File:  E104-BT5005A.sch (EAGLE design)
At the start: 5 parts

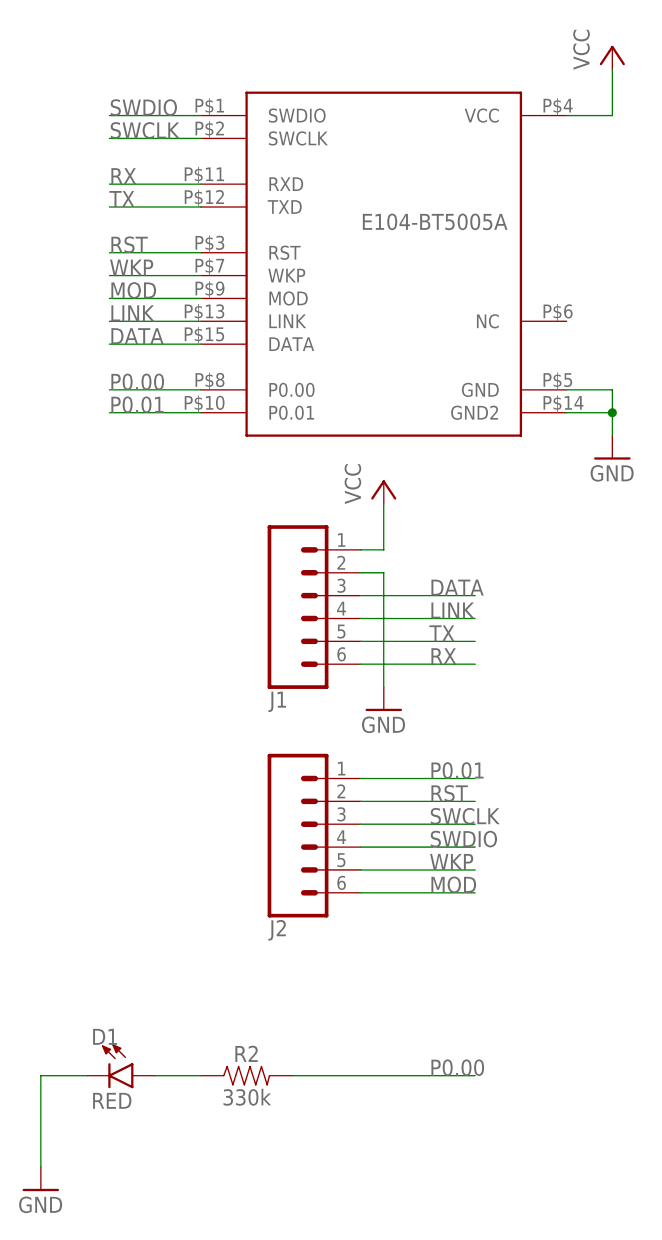
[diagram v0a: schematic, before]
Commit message: v2 fixes, errors with part library
the original module library had errors. fixed module and silkscreen, added eagle library for ble module
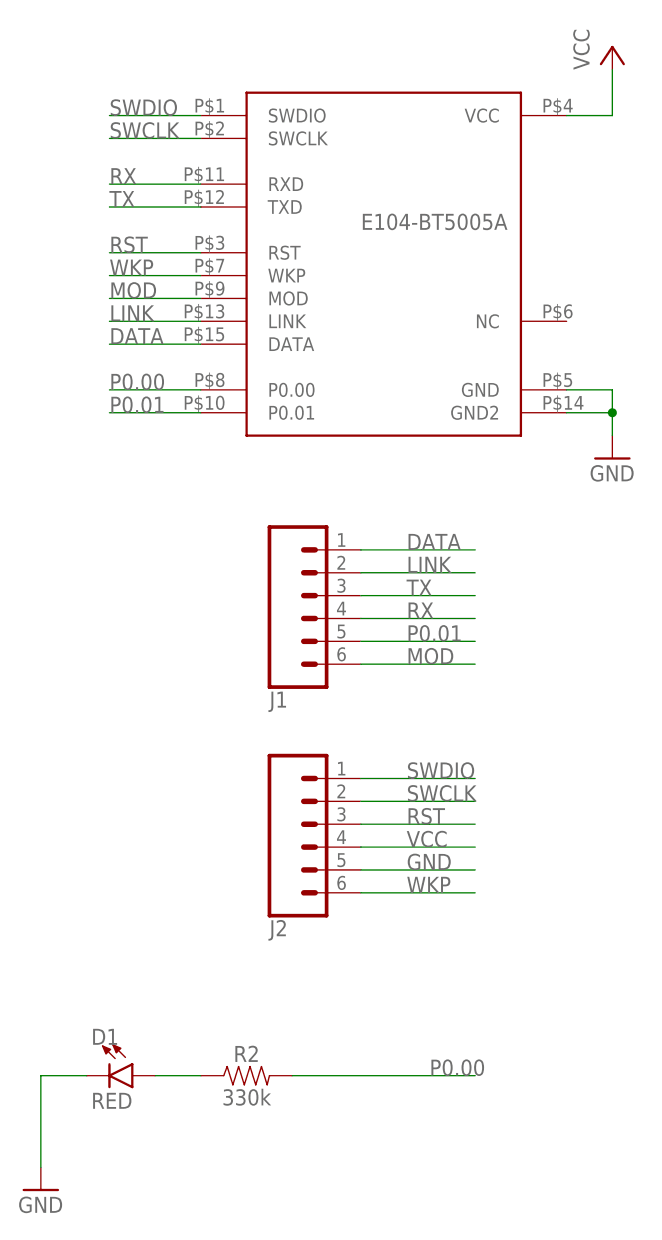
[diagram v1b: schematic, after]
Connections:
- net DATA: now also J1.1; no longer J1.3
- net GND: now also J2.5; no longer J1.2
- net LINK: now also J1.2; no longer J1.4
- net MOD: now also J1.6; no longer J2.6
- net P0.01: now also J1.5; no longer J2.1
- net RST: now also J2.3; no longer J2.2
- net RX: now also J1.4; no longer J1.6
- net SWCLK: now also J2.2; no longer J2.3
- net SWDIO: now also J2.1; no longer J2.4
- net TX: now also J1.3; no longer J1.5
- net VCC: now also J2.4; no longer J1.1
- net WKP: now also J2.6; no longer J2.5
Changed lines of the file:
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@@
 <part name="GND1" library="supply1" library_urn="urn:adsk.eagle:library:371" deviceset="GND" device=""/>
 <part name="J1" library="SparkFun-Connectors" library_urn="urn:adsk.eagle:library:513" deviceset="CONN_06" device="SILK_FEMALE_PTH" package3d_urn="urn:adsk.eagle:package:38009/1"/>
-<part name="P+2" library="supply1" library_urn="urn:adsk.eagle:library:371" deviceset="VCC" device=""/>
-<part name="GND2" library="supply1" library_urn="urn:adsk.eagle:library:371" deviceset="GND" device=""/>
 <part name="J2" library="SparkFun-Connectors" library_urn="urn:adsk.eagle:library:513" deviceset="CONN_06" device="SILK_FEMALE_PTH" package3d_urn="urn:adsk.eagle:package:38009/1"/>
 <part name="R2" library="SparkFun-Resistors" library_urn="urn:adsk.eagle:library:532" deviceset="330KOHM" device="-0603-1/10W-1%" package3d_urn="urn:adsk.eagle:package:39650/1" value="330k"/>
@@
 <attribute name="NAME" x="5.08" y="-25.908" size="1.778" layer="95" font="vector" rot="MR180"/>
 </instance>
-<instance part="P+2" gate="VCC" x="17.78" y="-2.54" smashed="yes">
-<attribute name="VALUE" x="15.24" y="-5.08" size="1.778" layer="96" rot="R90"/>
-</instance>
-<instance part="GND2" gate="1" x="17.78" y="-27.94" smashed="yes">
-<attribute name="VALUE" x="15.24" y="-30.48" size="1.778" layer="96"/>
-</instance>
 <instance part="J2" gate="G$1" x="10.16" y="-40.64" smashed="yes" rot="MR180">
 <attribute name="VALUE" x="5.08" y="-30.734" size="1.778" layer="96" font="vector" rot="MR180"/>
@@
 </segment>
 <segment>
-<pinref part="J1" gate="G$1" pin="1"/>
-<wire x1="15.24" y1="-10.16" x2="17.78" y2="-10.16" width="0.1524" layer="91"/>
-<pinref part="P+2" gate="VCC" pin="VCC"/>
-<wire x1="17.78" y1="-10.16" x2="17.78" y2="-5.08" width="0.1524" layer="91"/>
+<pinref part="J2" gate="G$1" pin="4"/>
+<wire x1="15.24" y1="-43.18" x2="27.94" y2="-43.18" width="0.1524" layer="91"/>
+<label x="20.32" y="-43.18" size="1.778" layer="95"/>
 </segment>
 </net>
@@
 </segment>
 <segment>
-<pinref part="GND2" gate="1" pin="GND"/>
-<wire x1="17.78" y1="-12.7" x2="17.78" y2="-25.4" width="0.1524" layer="91"/>
-<pinref part="J1" gate="G$1" pin="2"/>
-<wire x1="15.24" y1="-12.7" x2="17.78" y2="-12.7" width="0.1524" layer="91"/>
-</segment>
-<segment>
 <pinref part="D1" gate="G$1" pin="C"/>
 <wire x1="-15.24" y1="-68.58" x2="-20.32" y2="-68.58" width="0.1524" layer="91"/>
@@
 <wire x1="-20.32" y1="-68.58" x2="-20.32" y2="-78.74" width="0.1524" layer="91"/>
 </segment>
+<segment>
+<pinref part="J2" gate="G$1" pin="5"/>
+<wire x1="15.24" y1="-45.72" x2="27.94" y2="-45.72" width="0.1524" layer="91"/>
+<label x="20.32" y="-45.72" size="1.778" layer="95"/>
+</segment>
 </net>
 <net name="RX" class="0">
@@
 </segment>
 <segment>
-<pinref part="J1" gate="G$1" pin="6"/>
-<wire x1="15.24" y1="-22.86" x2="27.94" y2="-22.86" width="0.1524" layer="91"/>
-<label x="22.86" y="-22.86" size="1.778" layer="95"/>
+<pinref part="J1" gate="G$1" pin="4"/>
+<wire x1="15.24" y1="-17.78" x2="27.94" y2="-17.78" width="0.1524" layer="91"/>
+<label x="20.32" y="-17.78" size="1.778" layer="95"/>
 </segment>
 </net>
@@
 </segment>
 <segment>
-<pinref part="J1" gate="G$1" pin="5"/>
-<wire x1="15.24" y1="-20.32" x2="27.94" y2="-20.32" width="0.1524" layer="91"/>
-<label x="22.86" y="-20.32" size="1.778" layer="95"/>
+<pinref part="J1" gate="G$1" pin="3"/>
+<wire x1="15.24" y1="-15.24" x2="27.94" y2="-15.24" width="0.1524" layer="91"/>
+<label x="20.32" y="-15.24" size="1.778" layer="95"/>
 </segment>
 </net>
@@
 </segment>
 <segment>
-<pinref part="J2" gate="G$1" pin="2"/>
-<wire x1="15.24" y1="-38.1" x2="27.94" y2="-38.1" width="0.1524" layer="91"/>
-<label x="22.86" y="-38.1" size="1.778" layer="95"/>
+<pinref part="J2" gate="G$1" pin="3"/>
+<wire x1="15.24" y1="-40.64" x2="27.94" y2="-40.64" width="0.1524" layer="91"/>
+<label x="20.32" y="-40.64" size="1.778" layer="95"/>
 </segment>
 </net>
@@
 </segment>
 <segment>
-<pinref part="J1" gate="G$1" pin="4"/>
-<wire x1="15.24" y1="-17.78" x2="27.94" y2="-17.78" width="0.1524" layer="91"/>
-<label x="22.86" y="-17.78" size="1.778" layer="95"/>
+<pinref part="J1" gate="G$1" pin="2"/>
+<wire x1="15.24" y1="-12.7" x2="27.94" y2="-12.7" width="0.1524" layer="91"/>
+<label x="20.32" y="-12.7" size="1.778" layer="95"/>
 </segment>
 </net>
@@
 </segment>
 <segment>
-<pinref part="J2" gate="G$1" pin="5"/>
-<wire x1="15.24" y1="-45.72" x2="27.94" y2="-45.72" width="0.1524" layer="91"/>
-<label x="22.86" y="-45.72" size="1.778" layer="95"/>
+<pinref part="J2" gate="G$1" pin="6"/>
+<wire x1="15.24" y1="-48.26" x2="27.94" y2="-48.26" width="0.1524" layer="91"/>
+<label x="20.32" y="-48.26" size="1.778" layer="95"/>
 </segment>
 </net>
@@
 </segment>
 <segment>
-<pinref part="J2" gate="G$1" pin="6"/>
-<wire x1="15.24" y1="-48.26" x2="27.94" y2="-48.26" width="0.1524" layer="91"/>
-<label x="22.86" y="-48.26" size="1.778" layer="95"/>
+<pinref part="J1" gate="G$1" pin="6"/>
+<wire x1="15.24" y1="-22.86" x2="27.94" y2="-22.86" width="0.1524" layer="91"/>
+<label x="20.32" y="-22.86" size="1.778" layer="95"/>
 </segment>
 </net>
@@
 </segment>
 <segment>
-<pinref part="J1" gate="G$1" pin="3"/>
-<wire x1="15.24" y1="-15.24" x2="27.94" y2="-15.24" width="0.1524" layer="91"/>
-<label x="22.86" y="-15.24" size="1.778" layer="95"/>
+<pinref part="J1" gate="G$1" pin="1"/>
+<wire x1="15.24" y1="-10.16" x2="27.94" y2="-10.16" width="0.1524" layer="91"/>
+<label x="20.32" y="-10.16" size="1.778" layer="95"/>
 </segment>
 </net>
@@
 </segment>
 <segment>
-<pinref part="J2" gate="G$1" pin="4"/>
-<wire x1="15.24" y1="-43.18" x2="27.94" y2="-43.18" width="0.1524" layer="91"/>
-<label x="22.86" y="-43.18" size="1.778" layer="95"/>
+<pinref part="J2" gate="G$1" pin="1"/>
+<wire x1="15.24" y1="-35.56" x2="27.94" y2="-35.56" width="0.1524" layer="91"/>
+<label x="20.32" y="-35.56" size="1.778" layer="95"/>
 </segment>
 </net>
@@
 </segment>
 <segment>
-<pinref part="J2" gate="G$1" pin="3"/>
-<wire x1="15.24" y1="-40.64" x2="27.94" y2="-40.64" width="0.1524" layer="91"/>
-<label x="22.86" y="-40.64" size="1.778" layer="95"/>
+<pinref part="J2" gate="G$1" pin="2"/>
+<wire x1="15.24" y1="-38.1" x2="27.94" y2="-38.1" width="0.1524" layer="91"/>
+<label x="20.32" y="-38.1" size="1.778" layer="95"/>
 </segment>
 </net>
@@
 </segment>
 <segment>
-<pinref part="J2" gate="G$1" pin="1"/>
-<wire x1="15.24" y1="-35.56" x2="27.94" y2="-35.56" width="0.1524" layer="91"/>
-<label x="22.86" y="-35.56" size="1.778" layer="95"/>
-</segment>
-</net>
+<pinref part="J1" gate="G$1" pin="5"/>
+<wire x1="15.24" y1="-20.32" x2="27.94" y2="-20.32" width="0.1524" layer="91"/>
+<label x="20.32" y="-20.32" size="1.778" layer="95"/>
+</segment>
+</net>
